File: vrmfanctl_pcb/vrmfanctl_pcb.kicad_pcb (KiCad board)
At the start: 2 copper layers, 25.6 x 20.6 mm, 11 parts, among them J1 SATA Power Male, J3 Pin header L-type male, J4 Pin header L-type female, Q1 ?, U1 ATtiny85-20PU

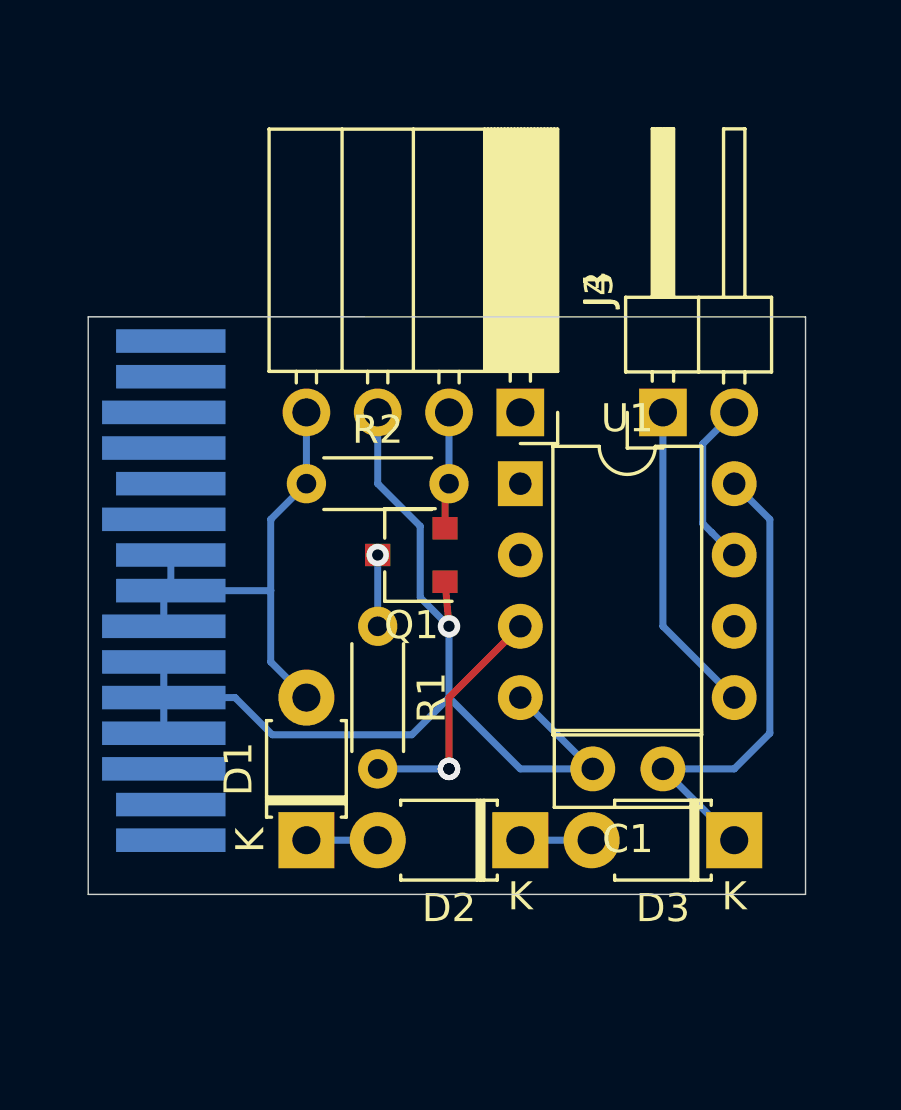
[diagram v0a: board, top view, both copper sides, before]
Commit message: forgot to wire FG
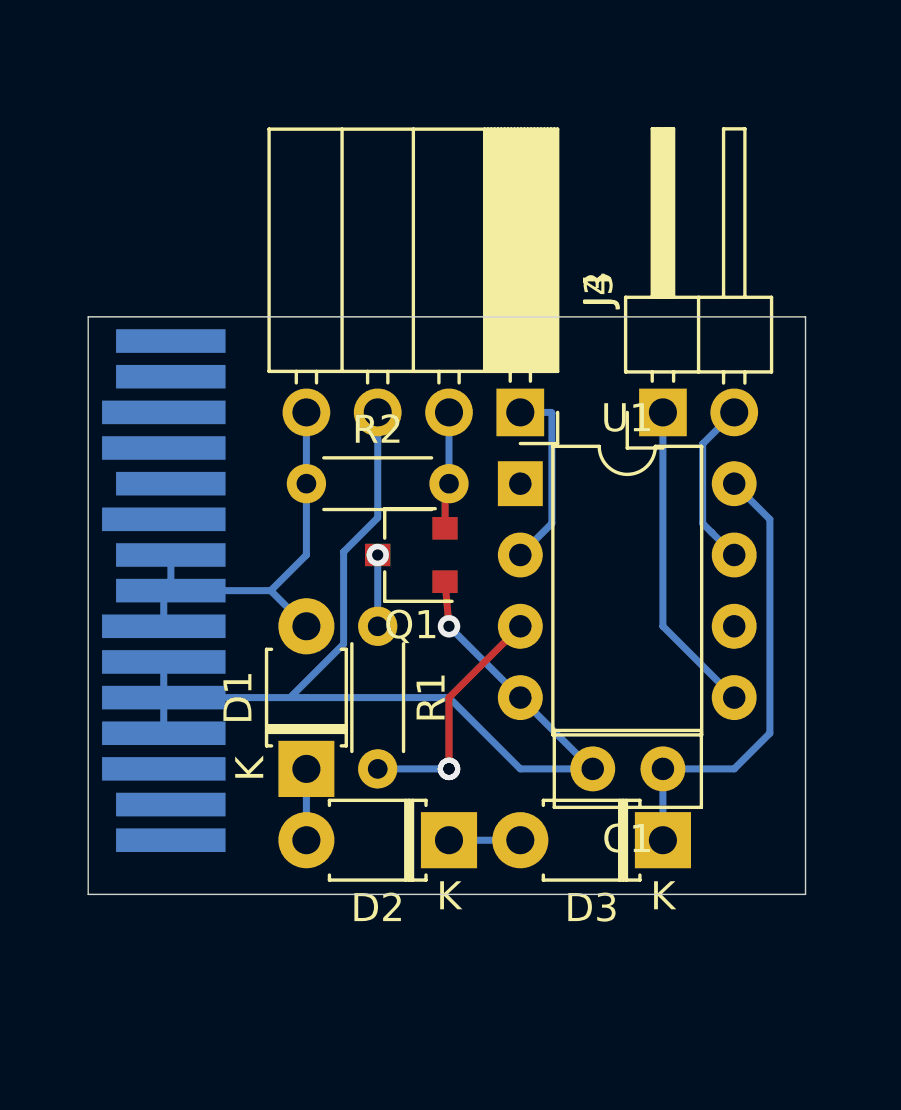
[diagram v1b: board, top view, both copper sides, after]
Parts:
- moved D2 2.54 mm to (50.8, 61.0)
- moved D1 2.54 mm to (45.7, 58.4)
- moved D3 2.54 mm to (58.4, 61.0)
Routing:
- net /FG: track 0.00 -> 6.66 mm
- net GND: track 36.9 -> 39.6 mm
- net /5V: track 20.0 -> 17.4 mm
- net VCC: track 17.3 -> 16.3 mm
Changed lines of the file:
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@@
     (thickness 1.6)
     (drawings 4)
-    (tracks 57)
+    (tracks 60)
     (zones 0)
     (modules 11)
@@
   )
   (module Diode_THT:D_T-1_P5.08mm_Horizontal (layer F.Cu)
-    (at 45.72 60.96 90)
+    (at 45.72 58.42 90)
     (descr "Diode, T-1 series, Axial, Horizontal, pin pitch=5.08mm, , length*diameter=3.2*2.6mm^2, , http://www.diodes.com/_files/packages/T-1.pdf")
     (tags "Diode T-1 series Axial Horizontal pin pitch 5.08mm  length 3.2mm diameter 2.6mm")
@@
   )
   (module Diode_THT:D_T-1_P5.08mm_Horizontal (layer F.Cu)
-    (at 53.34 60.96 180)
+    (at 50.8 60.96 180)
     (descr "Diode, T-1 series, Axial, Horizontal, pin pitch=5.08mm, , length*diameter=3.2*2.6mm^2, , http://www.diodes.com/_files/packages/T-1.pdf")
     (tags "Diode T-1 series Axial Horizontal pin pitch 5.08mm  length 3.2mm diameter 2.6mm")
@@
   )
   (module Diode_THT:D_T-1_P5.08mm_Horizontal (layer F.Cu)
-    (at 60.96 60.96 180)
+    (at 58.42 60.96 180)
     (descr "Diode, T-1 series, Axial, Horizontal, pin pitch=5.08mm, , length*diameter=3.2*2.6mm^2, , http://www.diodes.com/_files/packages/T-1.pdf")
     (tags "Diode T-1 series Axial Horizontal pin pitch 5.08mm  length 3.2mm diameter 2.6mm")
@@
   (gr_line (start 63.5 62.8904) (end 37.9476 62.8904) (layer Edge.Cuts) (width 0.05))
   (gr_line (start 63.5 62.8904) (end 63.5 42.3164) (layer Edge.Cuts) (width 0.05))
-  (segment (start 60.96 60.96) (end 58.42 58.42) (width 0.25) (layer B.Cu) (net 1))
   (segment (start 60.96 58.42) (end 58.42 58.42) (width 0.25) (layer B.Cu) (net 1))
   (segment (start 60.96 48.26) (end 62.23 49.53) (width 0.25) (layer B.Cu) (net 1))
   (segment (start 62.23 49.53) (end 62.23 57.15) (width 0.25) (layer B.Cu) (net 1))
   (segment (start 62.23 57.15) (end 60.96 58.42) (width 0.25) (layer B.Cu) (net 1))
+  (segment (start 58.42 60.96) (end 58.42 58.42) (width 0.25) (layer B.Cu) (net 1))
   (segment (start 40.64 57.15) (end 40.64 55.88) (width 0.25) (layer B.Cu) (net 2) (status 30))
   (segment (start 40.64 54.61) (end 40.64 55.88) (width 0.25) (layer B.Cu) (net 2) (status 30))
@@
   (via (at 50.8 53.34) (size 0.8) (drill 0.4) (layers F.Cu B.Cu) (net 2))
   (segment (start 40.64 55.88) (end 43.18 55.88) (width 0.25) (layer B.Cu) (net 2))
-  (segment (start 50.8 55.88) (end 53.34 58.42) (width 0.25) (layer B.Cu) (net 2))
-  (segment (start 50.8 53.34) (end 50.8 55.88) (width 0.25) (layer B.Cu) (net 2))
-  (segment (start 49.474999 57.205001) (end 50.8 55.88) (width 0.25) (layer B.Cu) (net 2))
-  (segment (start 44.505001 57.205001) (end 49.474999 57.205001) (width 0.25) (layer B.Cu) (net 2))
-  (segment (start 43.18 55.88) (end 44.505001 57.205001) (width 0.25) (layer B.Cu) (net 2))
   (segment (start 50.61 51.75) (end 50.66 51.75) (width 0.25) (layer F.Cu) (net 2))
-  (segment (start 49.774999 52.314999) (end 49.774999 49.774999) (width 0.25) (layer B.Cu) (net 2))
-  (segment (start 50.8 53.34) (end 49.774999 52.314999) (width 0.25) (layer B.Cu) (net 2))
-  (segment (start 48.26 48.26) (end 48.26 45.72) (width 0.25) (layer B.Cu) (net 2))
-  (segment (start 49.774999 49.774999) (end 48.26 48.26) (width 0.25) (layer B.Cu) (net 2))
   (segment (start 53.34 58.42) (end 55.92 58.42) (width 0.25) (layer B.Cu) (net 2))
   (segment (start 55.88 58.42) (end 55.92 58.42) (width 0.25) (layer B.Cu) (net 2))
   (segment (start 53.34 55.88) (end 55.88 58.42) (width 0.25) (layer B.Cu) (net 2))
+  (segment (start 45.141002 55.88) (end 43.18 55.88) (width 0.25) (layer B.Cu) (net 2))
+  (segment (start 53.34 58.42) (end 50.8 55.88) (width 0.25) (layer B.Cu) (net 2))
+  (segment (start 50.8 55.88) (end 45.72 55.88) (width 0.25) (layer B.Cu) (net 2))
+  (segment (start 45.72 55.88) (end 45.141002 55.88) (width 0.25) (layer B.Cu) (net 2))
+  (segment (start 47.045001 53.976001) (end 45.141002 55.88) (width 0.25) (layer B.Cu) (net 2))
+  (segment (start 47.045001 50.689998) (end 47.045001 53.976001) (width 0.25) (layer B.Cu) (net 2))
+  (segment (start 48.26 45.72) (end 48.26 49.474999) (width 0.25) (layer B.Cu) (net 2))
+  (segment (start 48.26 49.474999) (end 47.045001 50.689998) (width 0.25) (layer B.Cu) (net 2))
+  (segment (start 50.8 53.34) (end 53.34 55.88) (width 0.25) (layer B.Cu) (net 2))
   (segment (start 58.42 53.34) (end 60.96 55.88) (width 0.25) (layer B.Cu) (net 12))
   (segment (start 58.42 45.72) (end 58.42 53.34) (width 0.25) (layer B.Cu) (net 12))
@@
   (segment (start 60.160001 50.000001) (end 60.96 50.8) (width 0.25) (layer B.Cu) (net 13))
   (segment (start 60.96 45.72) (end 59.834999 46.845001) (width 0.25) (layer B.Cu) (net 13))
-  (segment (start 48.26 60.96) (end 45.72 60.96) (width 0.25) (layer B.Cu) (net 17))
+  (segment (start 54.44 45.72) (end 53.34 45.72) (width 0.25) (layer B.Cu) (net 14))
+  (segment (start 54.465001 45.745001) (end 54.44 45.72) (width 0.25) (layer B.Cu) (net 14))
+  (segment (start 54.465001 49.674999) (end 54.465001 45.745001) (width 0.25) (layer B.Cu) (net 14))
+  (segment (start 53.34 50.8) (end 54.465001 49.674999) (width 0.25) (layer B.Cu) (net 14))
+  (segment (start 45.72 58.42) (end 45.72 60.96) (width 0.25) (layer B.Cu) (net 17))
   (segment (start 40.89 50.8) (end 40.89 52.07) (width 0.25) (layer B.Cu) (net 18))
   (segment (start 40.64 52.32) (end 40.89 52.07) (width 0.25) (layer B.Cu) (net 18))
   (segment (start 40.64 53.34) (end 40.64 52.32) (width 0.25) (layer B.Cu) (net 18))
   (segment (start 41.91 52.07) (end 40.89 52.07) (width 0.25) (layer B.Cu) (net 18))
+  (segment (start 45.72 45.72) (end 45.72 48.26) (width 0.25) (layer B.Cu) (net 18))
   (segment (start 42.42 52.07) (end 40.89 52.07) (width 0.25) (layer B.Cu) (net 18))
-  (segment (start 44.45 52.07) (end 40.89 52.07) (width 0.25) (layer B.Cu) (net 18))
-  (segment (start 44.45 54.61) (end 45.72 55.88) (width 0.25) (layer B.Cu) (net 18))
-  (segment (start 44.45 52.07) (end 44.45 54.61) (width 0.25) (layer B.Cu) (net 18))
-  (segment (start 45.72 45.72) (end 45.72 48.26) (width 0.25) (layer B.Cu) (net 18))
-  (segment (start 44.45 49.53) (end 45.72 48.26) (width 0.25) (layer B.Cu) (net 18))
-  (segment (start 44.45 52.07) (end 44.45 49.53) (width 0.25) (layer B.Cu) (net 18))
-  (segment (start 55.88 60.96) (end 53.34 60.96) (width 0.25) (layer B.Cu) (net 19))
+  (segment (start 44.45 52.07) (end 45.72 53.34) (width 0.25) (layer B.Cu) (net 18))
+  (segment (start 40.89 52.07) (end 44.45 52.07) (width 0.25) (layer B.Cu) (net 18))
+  (segment (start 44.45 52.07) (end 45.72 50.8) (width 0.25) (layer B.Cu) (net 18))
+  (segment (start 45.72 50.8) (end 45.72 48.26) (width 0.25) (layer B.Cu) (net 18))
+  (segment (start 50.8 60.96) (end 53.34 60.96) (width 0.25) (layer B.Cu) (net 19))
   (segment (start 48.26 50.8) (end 48.26 50.8) (width 0.25) (layer B.Cu) (net 20))
   (via (at 48.26 50.8) (size 0.8) (drill 0.4) (layers F.Cu B.Cu) (net 20))

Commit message: Use OC1A instead of OC1B. OC1B PWM output of ATTiny85 has a problem the same as ATTiny45 Rev B-C.
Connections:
- U1 pad 3: /PWM# -> Net-(U1-Pad3)
- U1 pad 6: Net-(U1-Pad6) -> /PWM#
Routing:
- net /PWM#: track 8.67 -> 14.8 mm
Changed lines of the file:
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@@
-(kicad_pcb (version 20171130) (host pcbnew 5.1.4-e60b266~84~ubuntu18.04.1)
+(kicad_pcb (version 20171130) (host pcbnew 5.0.2+dfsg1-1)
   (general
     (thickness 1.6)
     (drawings 4)
-    (tracks 60)
+    (tracks 62)
     (zones 0)
     (modules 11)
@@
     (zone_45_only no)
     (trace_min 0.2)
+    (segment_width 0.2)
+    (edge_width 0.05)
     (via_size 0.8)
     (via_drill 0.4)
@@
     (uvia_min_size 0.2)
     (uvia_min_drill 0.1)
-    (edge_width 0.05)
-    (segment_width 0.2)
     (pcb_text_width 0.3)
     (pcb_text_size 1.5 1.5)
@@
   (net 14 /FG)
   (net 15 "Net-(U1-Pad1)")
-  (net 16 "Net-(U1-Pad6)")
-  (net 17 "Net-(D1-Pad1)")
-  (net 18 /5V)
-  (net 19 "Net-(D2-Pad1)")
-  (net 20 "Net-(Q1-Pad3)")
-  (net 21 /PWM#)
-  (net 22 /PWM_5V)
+  (net 16 "Net-(D1-Pad1)")
+  (net 17 /5V)
+  (net 18 "Net-(D2-Pad1)")
+  (net 19 "Net-(Q1-Pad3)")
+  (net 20 /PWM#)
+  (net 21 /PWM_5V)
+  (net 22 "Net-(U1-Pad3)")
   (net_class Default "これはデフォルトのネット クラスです。"
     (clearance 0.2)
@@
     (add_net "Net-(Q1-Pad3)")
     (add_net "Net-(U1-Pad1)")
-    (add_net "Net-(U1-Pad6)")
+    (add_net "Net-(U1-Pad3)")
     (add_net VCC)
   )
@@
     (fp_line (start -10.03 -1.27) (end -2.49 -1.27) (layer F.Fab) (width 0.1))
     (pad 4 thru_hole oval (at 0 7.62 270) (size 1.7 1.7) (drill 1) (layers *.Cu *.Mask)
-      (net 18 /5V))
+      (net 17 /5V))
     (pad 3 thru_hole oval (at 0 5.08 270) (size 1.7 1.7) (drill 1) (layers *.Cu *.Mask)
       (net 2 GND))
     (pad 2 thru_hole oval (at 0 2.54 270) (size 1.7 1.7) (drill 1) (layers *.Cu *.Mask)
-      (net 22 /PWM_5V))
+      (net 21 /PWM_5V))
     (pad 1 thru_hole rect (at 0 0 270) (size 1.7 1.7) (drill 1) (layers *.Cu *.Mask)
       (net 14 /FG))
@@
       (net 6 "Net-(J1-Pad10)"))
     (pad 9 smd rect (at -10.58 1.95 270) (size 0.84 3.9) (layers B.Cu B.Paste B.Mask)
-      (net 18 /5V))
+      (net 17 /5V))
     (pad 8 smd rect (at -9.31 1.95 270) (size 0.84 3.9) (layers B.Cu B.Paste B.Mask)
-      (net 18 /5V))
+      (net 17 /5V))
     (pad 7 smd rect (at -8.04 2.2 270) (size 0.84 4.4) (layers B.Cu B.Paste B.Mask)
-      (net 18 /5V))
+      (net 17 /5V))
     (pad 6 smd rect (at -6.77 2.2 270) (size 0.84 4.4) (layers B.Cu B.Paste B.Mask)
       (net 2 GND))
@@
       (net 13 /SCL))
     (pad 3 thru_hole oval (at 0 5.08) (size 1.6 1.6) (drill 0.8) (layers *.Cu *.Mask)
-      (net 21 /PWM#))
+      (net 22 "Net-(U1-Pad3)"))
     (pad 6 thru_hole oval (at 7.62 5.08) (size 1.6 1.6) (drill 0.8) (layers *.Cu *.Mask)
-      (net 16 "Net-(U1-Pad6)"))
+      (net 20 /PWM#))
     (pad 2 thru_hole oval (at 0 2.54) (size 1.6 1.6) (drill 0.8) (layers *.Cu *.Mask)
       (net 14 /FG))
@@
     )
     (pad 1 thru_hole rect (at 0 0 90) (size 2 2) (drill 1) (layers *.Cu *.Mask)
-      (net 17 "Net-(D1-Pad1)"))
+      (net 16 "Net-(D1-Pad1)"))
     (pad 2 thru_hole oval (at 5.08 0 90) (size 2 2) (drill 1) (layers *.Cu *.Mask)
-      (net 18 /5V))
+      (net 17 /5V))
     (model ${KISYS3DMOD}/Diode_THT.3dshapes/D_T-1_P5.08mm_Horizontal.wrl
       (at (xyz 0 0 0))
@@
     (fp_line (start 0.94 -1.3) (end 0.94 1.3) (layer F.Fab) (width 0.1))
     (pad 2 thru_hole oval (at 5.08 0 180) (size 2 2) (drill 1) (layers *.Cu *.Mask)
-      (net 17 "Net-(D1-Pad1)"))
+      (net 16 "Net-(D1-Pad1)"))
     (pad 1 thru_hole rect (at 0 0 180) (size 2 2) (drill 1) (layers *.Cu *.Mask)
-      (net 19 "Net-(D2-Pad1)"))
+      (net 18 "Net-(D2-Pad1)"))
     (model ${KISYS3DMOD}/Diode_THT.3dshapes/D_T-1_P5.08mm_Horizontal.wrl
       (at (xyz 0 0 0))
@@
       (net 1 VCC))
     (pad 2 thru_hole oval (at 5.08 0 180) (size 2 2) (drill 1) (layers *.Cu *.Mask)
-      (net 19 "Net-(D2-Pad1)"))
+      (net 18 "Net-(D2-Pad1)"))
     (model ${KISYS3DMOD}/Diode_THT.3dshapes/D_T-1_P5.08mm_Horizontal.wrl
       (at (xyz 0 0 0))
@@
       (net 2 GND))
     (pad 2 smd rect (at -1.2 0.95 180) (size 0.9 0.8) (layers F.Cu F.Paste F.Mask)
-      (net 22 /PWM_5V))
+      (net 21 /PWM_5V))
     (pad 3 smd rect (at 1.2 0 180) (size 0.9 0.8) (layers F.Cu F.Paste F.Mask)
-      (net 20 "Net-(Q1-Pad3)"))
+      (net 19 "Net-(Q1-Pad3)"))
     (model ${KISYS3DMOD}/Package_TO_SOT_SMD.3dshapes/SC-59.wrl
       (at (xyz 0 0 0))
@@
     )
     (pad 1 thru_hole circle (at 0 0 270) (size 1.4 1.4) (drill 0.7) (layers *.Cu *.Mask)
-      (net 20 "Net-(Q1-Pad3)"))
+      (net 19 "Net-(Q1-Pad3)"))
     (pad 2 thru_hole oval (at 5.08 0 270) (size 1.4 1.4) (drill 0.7) (layers *.Cu *.Mask)
-      (net 21 /PWM#))
+      (net 20 /PWM#))
     (model ${KISYS3DMOD}/Resistor_THT.3dshapes/R_Axial_DIN0204_L3.6mm_D1.6mm_P5.08mm_Horizontal.wrl
       (at (xyz 0 0 0))
@@
     )
     (pad 1 thru_hole circle (at 0 0) (size 1.4 1.4) (drill 0.7) (layers *.Cu *.Mask)
-      (net 18 /5V))
+      (net 17 /5V))
     (pad 2 thru_hole oval (at 5.08 0) (size 1.4 1.4) (drill 0.7) (layers *.Cu *.Mask)
-      (net 22 /PWM_5V))
+      (net 21 /PWM_5V))
     (model ${KISYS3DMOD}/Resistor_THT.3dshapes/R_Axial_DIN0204_L3.6mm_D1.6mm_P5.08mm_Horizontal.wrl
       (at (xyz 0 0 0))
@@
   (segment (start 54.465001 49.674999) (end 54.465001 45.745001) (width 0.25) (layer B.Cu) (net 14))
   (segment (start 53.34 50.8) (end 54.465001 49.674999) (width 0.25) (layer B.Cu) (net 14))
-  (segment (start 45.72 58.42) (end 45.72 60.96) (width 0.25) (layer B.Cu) (net 17))
-  (segment (start 40.89 50.8) (end 40.89 52.07) (width 0.25) (layer B.Cu) (net 18))
-  (segment (start 40.64 52.32) (end 40.89 52.07) (width 0.25) (layer B.Cu) (net 18))
-  (segment (start 40.64 53.34) (end 40.64 52.32) (width 0.25) (layer B.Cu) (net 18))
-  (segment (start 41.91 52.07) (end 40.89 52.07) (width 0.25) (layer B.Cu) (net 18))
-  (segment (start 45.72 45.72) (end 45.72 48.26) (width 0.25) (layer B.Cu) (net 18))
-  (segment (start 42.42 52.07) (end 40.89 52.07) (width 0.25) (layer B.Cu) (net 18))
-  (segment (start 44.45 52.07) (end 45.72 53.34) (width 0.25) (layer B.Cu) (net 18))
-  (segment (start 40.89 52.07) (end 44.45 52.07) (width 0.25) (layer B.Cu) (net 18))
-  (segment (start 44.45 52.07) (end 45.72 50.8) (width 0.25) (layer B.Cu) (net 18))
-  (segment (start 45.72 50.8) (end 45.72 48.26) (width 0.25) (layer B.Cu) (net 18))
-  (segment (start 50.8 60.96) (end 53.34 60.96) (width 0.25) (layer B.Cu) (net 19))
-  (segment (start 48.26 50.8) (end 48.26 50.8) (width 0.25) (layer B.Cu) (net 20))
-  (via (at 48.26 50.8) (size 0.8) (drill 0.4) (layers F.Cu B.Cu) (net 20))
-  (segment (start 48.26 50.8) (end 48.26 53.34) (width 0.25) (layer B.Cu) (net 20))
-  (segment (start 48.26 58.42) (end 50.8 58.42) (width 0.25) (layer B.Cu) (net 21))
-  (segment (start 50.8 58.42) (end 50.8 58.42) (width 0.25) (layer B.Cu) (net 21))
-  (via (at 50.8 58.42) (size 0.8) (drill 0.4) (layers F.Cu B.Cu) (net 21))
-  (segment (start 50.8 58.42) (end 50.8 58.42) (width 0.25) (layer B.Cu) (net 21))
-  (via (at 50.8 58.42) (size 0.8) (drill 0.4) (layers F.Cu B.Cu) (net 21))
-  (segment (start 50.8 55.88) (end 50.8 58.42) (width 0.25) (layer F.Cu) (net 21))
-  (segment (start 53.34 53.34) (end 50.8 55.88) (width 0.25) (layer F.Cu) (net 21))
-  (segment (start 50.66 48.4) (end 50.8 48.26) (width 0.25) (layer F.Cu) (net 22))
-  (segment (start 50.66 49.85) (end 50.66 48.4) (width 0.25) (layer F.Cu) (net 22))
-  (segment (start 50.8 48.26) (end 50.8 45.72) (width 0.25) (layer B.Cu) (net 22))
+  (segment (start 45.72 58.42) (end 45.72 60.96) (width 0.25) (layer B.Cu) (net 16))
+  (segment (start 40.89 50.8) (end 40.89 52.07) (width 0.25) (layer B.Cu) (net 17))
+  (segment (start 40.64 52.32) (end 40.89 52.07) (width 0.25) (layer B.Cu) (net 17))
+  (segment (start 40.64 53.34) (end 40.64 52.32) (width 0.25) (layer B.Cu) (net 17))
+  (segment (start 41.91 52.07) (end 40.89 52.07) (width 0.25) (layer B.Cu) (net 17))
+  (segment (start 45.72 45.72) (end 45.72 48.26) (width 0.25) (layer B.Cu) (net 17))
+  (segment (start 42.42 52.07) (end 40.89 52.07) (width 0.25) (layer B.Cu) (net 17))
+  (segment (start 44.45 52.07) (end 45.72 53.34) (width 0.25) (layer B.Cu) (net 17))
+  (segment (start 40.89 52.07) (end 44.45 52.07) (width 0.25) (layer B.Cu) (net 17))
+  (segment (start 44.45 52.07) (end 45.72 50.8) (width 0.25) (layer B.Cu) (net 17))
+  (segment (start 45.72 50.8) (end 45.72 48.26) (width 0.25) (layer B.Cu) (net 17))
+  (segment (start 50.8 60.96) (end 53.34 60.96) (width 0.25) (layer B.Cu) (net 18))
+  (segment (start 48.26 50.8) (end 48.26 50.8) (width 0.25) (layer B.Cu) (net 19))
+  (via (at 48.26 50.8) (size 0.8) (drill 0.4) (layers F.Cu B.Cu) (net 19))
+  (segment (start 48.26 50.8) (end 48.26 53.34) (width 0.25) (layer B.Cu) (net 19))
+  (segment (start 48.26 58.42) (end 50.8 58.42) (width 0.25) (layer B.Cu) (net 20))
+  (segment (start 50.8 58.42) (end 50.8 58.42) (width 0.25) (layer B.Cu) (net 20))
+  (via (at 50.8 58.42) (size 0.8) (drill 0.4) (layers F.Cu B.Cu) (net 20))
+  (segment (start 50.8 58.42) (end 50.8 58.42) (width 0.25) (layer B.Cu) (net 20))
+  (via (at 50.8 58.42) (size 0.8) (drill 0.4) (layers F.Cu B.Cu) (net 20))
+  (segment (start 60.160001 54.139999) (end 60.96 53.34) (width 0.25) (layer F.Cu) (net 20))
+  (segment (start 51.925001 57.294999) (end 57.005001 57.294999) (width 0.25) (layer F.Cu) (net 20))
+  (segment (start 57.005001 57.294999) (end 60.160001 54.139999) (width 0.25) (layer F.Cu) (net 20))
+  (segment (start 50.8 58.42) (end 51.925001 57.294999) (width 0.25) (layer F.Cu) (net 20))
+  (segment (start 50.66 48.4) (end 50.8 48.26) (width 0.25) (layer F.Cu) (net 21))
+  (segment (start 50.66 49.85) (end 50.66 48.4) (width 0.25) (layer F.Cu) (net 21))
+  (segment (start 50.8 48.26) (end 50.8 45.72) (width 0.25) (layer B.Cu) (net 21))
 )
